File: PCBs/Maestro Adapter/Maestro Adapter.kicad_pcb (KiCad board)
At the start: 2 copper layers, 44.9 x 45.8 mm, 24 parts

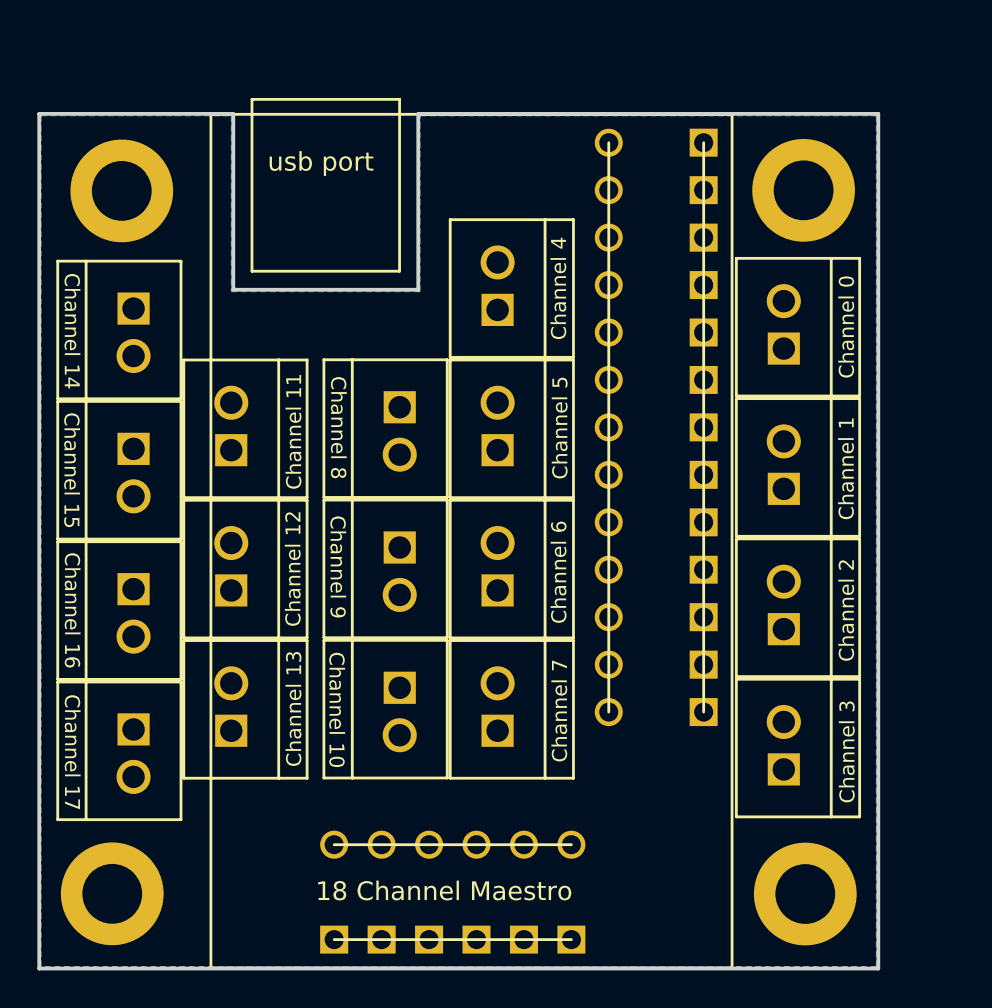
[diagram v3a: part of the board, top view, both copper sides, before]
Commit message: Added traces and rounded corners
mounting hole centers are 4mm from the side
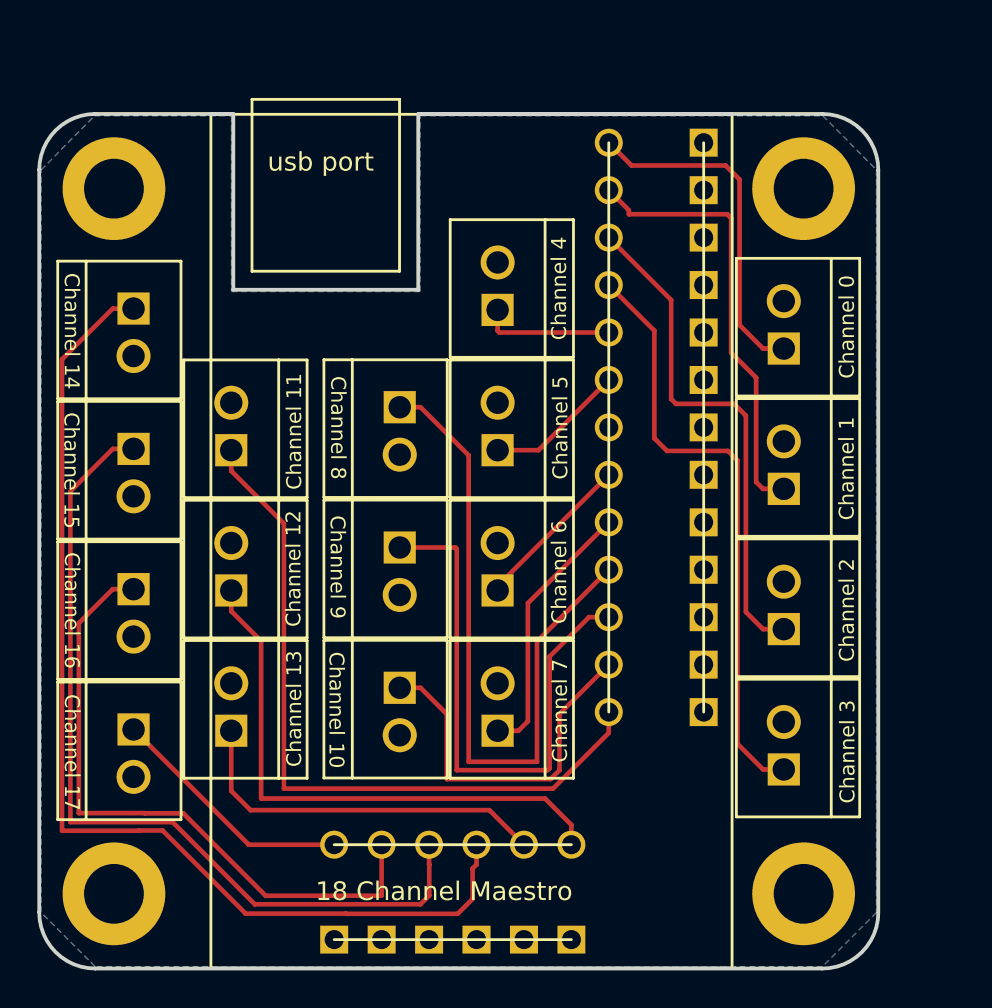
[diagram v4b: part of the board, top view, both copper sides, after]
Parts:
- moved ? 0.44 mm to (75.0, 126.5)
- moved ? 0.09 mm to (111.9, 164.3)
- moved ? 0.09 mm to (111.9, 126.5)
- moved ? 0.09 mm to (75.0, 164.3)
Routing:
- net Net-(J14-Pad1): track 0.00 -> 57.3 mm
- net Net-(J15-Pad1): track 0.00 -> 46.0 mm
- net Net-(J11-Pad1): track 0.00 -> 39.0 mm
- net Net-(J18-Pad10): track 0.00 -> 36.7 mm
- net Net-(J16-Pad1): track 0.00 -> 34.6 mm
- net Net-(J18-Pad4): track 0.00 -> 32.4 mm
- net Net-(J12-Pad1): track 0.00 -> 30.1 mm
- net Net-(J18-Pad11): track 0.00 -> 30.0 mm
- net Net-(J18-Pad3): track 0.00 -> 27.3 mm
- net Net-(J1-Pad1): track 0.00 -> 23.6 mm
- net Net-(J13-Pad1): track 0.00 -> 20.1 mm
- net Net-(J10-Pad1): track 0.00 -> 19.6 mm
- net Net-(J0-Pad1): track 0.00 -> 18.5 mm
- net Net-(J18-Pad9): track 0.00 -> 14.3 mm
- net Net-(J17-Pad1): track 0.00 -> 13.3 mm
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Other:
- outline, holes or cut-outs redrawn

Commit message: Added EER logo silkscreen
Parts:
- removed the ? at (169.0, 85.2)
- added ?: , through hole:EER silkscreen, F.Cu at (103.9, 161.4)

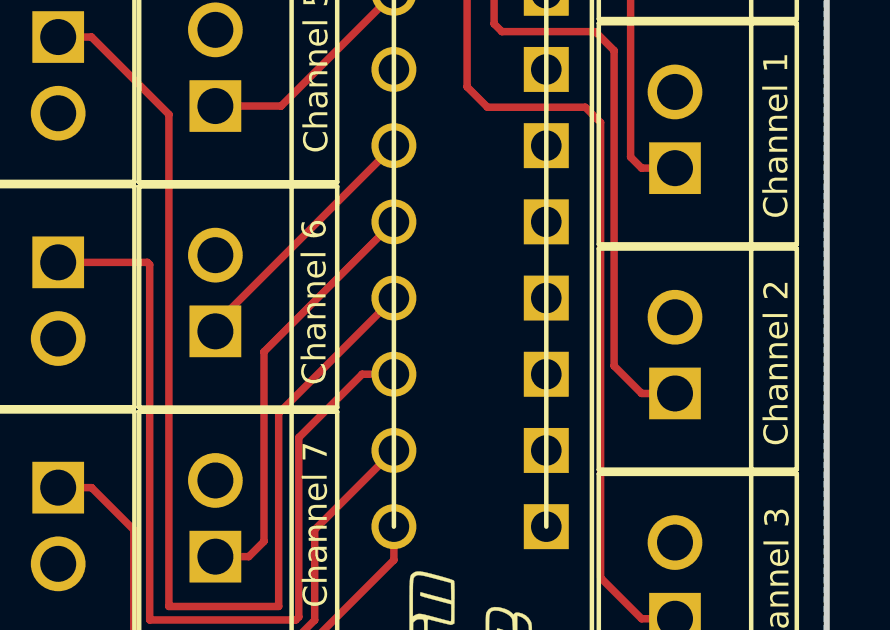
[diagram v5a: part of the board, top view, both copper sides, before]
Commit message: Added led and resistor pads
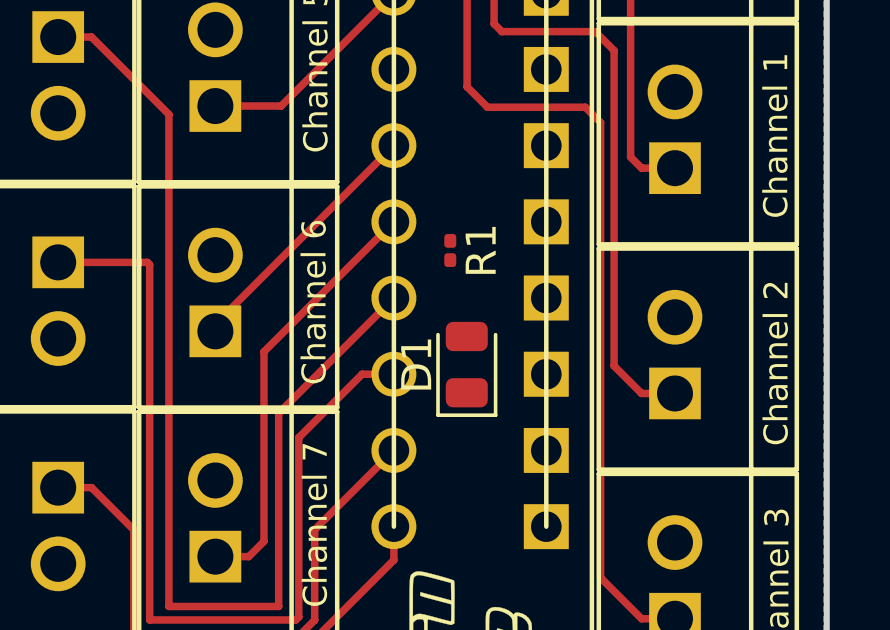
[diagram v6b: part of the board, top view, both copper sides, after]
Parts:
- added D1: LED, LED_SMD:LED_0805_2012Metric, F.Cu at (103.9, 149.1)
- added R1: R, Resistor_SMD:R_0201_0603Metric, F.Cu at (103.4, 145.3)
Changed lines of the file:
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@@
     (tracks 115)
     (zones 0)
-    (modules 24)
-    (nets 21)
+    (modules 26)
+    (nets 23)
   )
   (page A4)
@@
   (net 19 "Net-(J17-Pad1)")
   (net 20 "Net-(J18-Pad7)")
+  (net 21 "Net-(D1-Pad2)")
+  (net 22 +5V)
   (net_class Default "This is the default net class."
     (clearance 0.2)
@@
     (uvia_dia 0.3)
     (uvia_drill 0.1)
+    (add_net +5V)
     (add_net GND)
+    (add_net "Net-(D1-Pad2)")
     (add_net "Net-(J0-Pad1)")
     (add_net "Net-(J1-Pad1)")
@@
     (pad "" thru_hole circle (at 0 0) (size 5.5 5.5) (drill 3.2) (layers *.Cu *.Mask))
   )
+  (module LED_SMD:LED_0805_2012Metric (layer F.Cu)
+    (at 103.92 149.14 90)
+    (descr "LED SMD 0805 (2012 Metric), square (rectangular) end terminal, IPC_7351 nominal, (Body size source: https://docs.google.com/spreadsheets/d/1BsfQQcO9C6DZCsRaXUlFlo91Tg2WpOkGARC1WS5S8t0/edit?usp=sharing), generated with kicad-footprint-generator")
+    (tags diode)
+    (attr smd)
+    (fp_text reference D1 (at 0 -1.65 90) (layer F.SilkS)
+      (effects (font (size 1 1) (thickness 0.15)))
+    )
+    (fp_text value LED (at 0 1.65 90) (layer F.Fab)
+      (effects (font (size 1 1) (thickness 0.15)))
+    )
+    (fp_line (start 1 -0.6) (end -0.7 -0.6) (layer F.Fab) (width 0.1))
+    (fp_line (start -0.7 -0.6) (end -1 -0.3) (layer F.Fab) (width 0.1))
+    (fp_line (start -1 -0.3) (end -1 0.6) (layer F.Fab) (width 0.1))
+    (fp_line (start -1 0.6) (end 1 0.6) (layer F.Fab) (width 0.1))
+    (fp_line (start 1 0.6) (end 1 -0.6) (layer F.Fab) (width 0.1))
+    (fp_line (start 1 -0.96) (end -1.685 -0.96) (layer F.SilkS) (width 0.12))
+    (fp_line (start -1.685 -0.96) (end -1.685 0.96) (layer F.SilkS) (width 0.12))
+    (fp_line (start -1.685 0.96) (end 1 0.96) (layer F.SilkS) (width 0.12))
+    (fp_line (start -1.68 0.95) (end -1.68 -0.95) (layer F.CrtYd) (width 0.05))
+    (fp_line (start -1.68 -0.95) (end 1.68 -0.95) (layer F.CrtYd) (width 0.05))
+    (fp_line (start 1.68 -0.95) (end 1.68 0.95) (layer F.CrtYd) (width 0.05))
+    (fp_line (start 1.68 0.95) (end -1.68 0.95) (layer F.CrtYd) (width 0.05))
+    (fp_text user %R (at 0 0 90) (layer F.Fab)
+      (effects (font (size 0.5 0.5) (thickness 0.08)))
+    )
+    (pad 1 smd roundrect (at -0.9375 0 90) (size 0.975 1.4) (layers F.Cu F.Paste F.Mask) (roundrect_rratio 0.25)
+      (net 2 GND))
+    (pad 2 smd roundrect (at 0.9375 0 90) (size 0.975 1.4) (layers F.Cu F.Paste F.Mask) (roundrect_rratio 0.25)
+      (net 21 "Net-(D1-Pad2)"))
+    (model ${KISYS3DMOD}/LED_SMD.3dshapes/LED_0805_2012Metric.wrl
+      (at (xyz 0 0 0))
+      (scale (xyz 1 1 1))
+      (rotate (xyz 0 0 0))
+    )
+  )
+  (module Resistor_SMD:R_0201_0603Metric (layer F.Cu)
+    (at 103.37 145.335 270)
+    (descr "Resistor SMD 0201 (0603 Metric), square (rectangular) end terminal, IPC_7351 nominal, (Body size source: https://www.vishay.com/docs/20052/crcw0201e3.pdf), generated with kicad-footprint-generator")
+    (tags resistor)
+    (attr smd)
+    (fp_text reference R1 (at 0 -1.05 270) (layer F.SilkS)
+      (effects (font (size 1 1) (thickness 0.15)))
+    )
+    (fp_text value R (at 0 1.05 270) (layer F.Fab)
+      (effects (font (size 1 1) (thickness 0.15)))
+    )
+    (fp_line (start -0.3 0.15) (end -0.3 -0.15) (layer F.Fab) (width 0.1))
+    (fp_line (start -0.3 -0.15) (end 0.3 -0.15) (layer F.Fab) (width 0.1))
+    (fp_line (start 0.3 -0.15) (end 0.3 0.15) (layer F.Fab) (width 0.1))
+    (fp_line (start 0.3 0.15) (end -0.3 0.15) (layer F.Fab) (width 0.1))
+    (fp_line (start -0.7 0.35) (end -0.7 -0.35) (layer F.CrtYd) (width 0.05))
+    (fp_line (start -0.7 -0.35) (end 0.7 -0.35) (layer F.CrtYd) (width 0.05))
+    (fp_line (start 0.7 -0.35) (end 0.7 0.35) (layer F.CrtYd) (width 0.05))
+    (fp_line (start 0.7 0.35) (end -0.7 0.35) (layer F.CrtYd) (width 0.05))
+    (fp_text user %R (at 0 -0.68 270) (layer F.Fab)
+      (effects (font (size 0.25 0.25) (thickness 0.04)))
+    )
+    (pad "" smd roundrect (at -0.345 0 270) (size 0.318 0.36) (layers F.Paste) (roundrect_rratio 0.25))
+    (pad "" smd roundrect (at 0.345 0 270) (size 0.318 0.36) (layers F.Paste) (roundrect_rratio 0.25))
+    (pad 1 smd roundrect (at -0.32 0 270) (size 0.46 0.4) (layers F.Cu F.Mask) (roundrect_rratio 0.25)
+      (net 22 +5V))
+    (pad 2 smd roundrect (at 0.32 0 270) (size 0.46 0.4) (layers F.Cu F.Mask) (roundrect_rratio 0.25)
+      (net 21 "Net-(D1-Pad2)"))
+    (model ${KISYS3DMOD}/Resistor_SMD.3dshapes/R_0201_0603Metric.wrl
+      (at (xyz 0 0 0))
+      (scale (xyz 1 1 1))
+      (rotate (xyz 0 0 0))
+    )
+  )
   (gr_arc (start 112.92 165.27) (end 115.92 165.27) (angle 90) (layer Edge.Cuts) (width 0.2))

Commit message: Finalized the board
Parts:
- removed the ? at (111.9, 126.5)
- removed the ? at (75.0, 126.5)
- removed the ? at (75.0, 164.3)
- removed the ? at (111.9, 164.3)
- added ?: , through hole:Mi logo silkscreen, F.Cu at (104.0, 161.0)
- added ?: , through hole:Mun logo silkscreen, F.Cu at (104.1, 157.5)
- added ?: , Mounting_Holes:MountingHole_3.2mm_M3_Pad, F.Cu at (111.9, 126.5)
- added ?: , Mounting_Holes:MountingHole_3.2mm_M3_Pad, F.Cu at (75.0, 164.3)
- added ?: , Mounting_Holes:MountingHole_3.2mm_M3_Pad, F.Cu at (111.9, 164.3)
- added ?: , Mounting_Holes:MountingHole_3.2mm_M3_Pad, F.Cu at (75.0, 126.5)
- D1: footprint LED_SMD:LED_0805_2012Metric -> LEDs:LED_0805
- R1: footprint Resistor_SMD:R_0201_0603Metric -> Resistors_SMD:R_0603
- moved ? 3.04 mm to (104.0, 164.4), turned to 0 degrees
- moved D1 2.13 mm to (104.0, 147.0)
- moved R1 2.00 mm to (104.0, 143.4)
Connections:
- 18 Channel Maestro pad 7: Net-(J18-Pad7) -> +5V
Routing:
- net +5V: track 0.00 -> 4.44 mm
- net GND: track 0.00 -> 3.58 mm
- net Net-(J18-Pad11): track 30.0 -> 27.8 mm
- net Net-(D1-Pad2): track 0.00 -> 1.75 mm
- net Net-(J14-Pad1): track 57.3 -> 55.7 mm
- net Net-(J16-Pad1): track 34.6 -> 33.2 mm
- net Net-(J15-Pad1): track 46.0 -> 44.7 mm
- net Net-(J10-Pad1): track 19.6 -> 20.7 mm
- net Net-(J12-Pad1): track 30.1 -> 29.1 mm
- net Net-(J11-Pad1): track 39.0 -> 38.1 mm
- net Net-(J18-Pad10): track 36.7 -> 35.8 mm
- net Net-(J18-Pad5): track 7.10 -> 6.44 mm
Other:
- board text added: "18 Channel Maestro Adapter"
- board text added: "Created by: David Drover"

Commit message: Added text EER and year
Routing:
- net Net-(J15-Pad1): track 44.7 -> 43.0 mm
- net Net-(J16-Pad1): track 33.2 -> 31.7 mm
- net Net-(J14-Pad1): track 55.7 -> 54.9 mm
- net Net-(J13-Pad1): track 20.1 -> 19.5 mm
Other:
- rule via_min_size: 0.4 -> 0.3
- board text added: "Eastern Edge Robotics 2018/2019"
